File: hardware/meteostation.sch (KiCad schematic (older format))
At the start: 14 parts

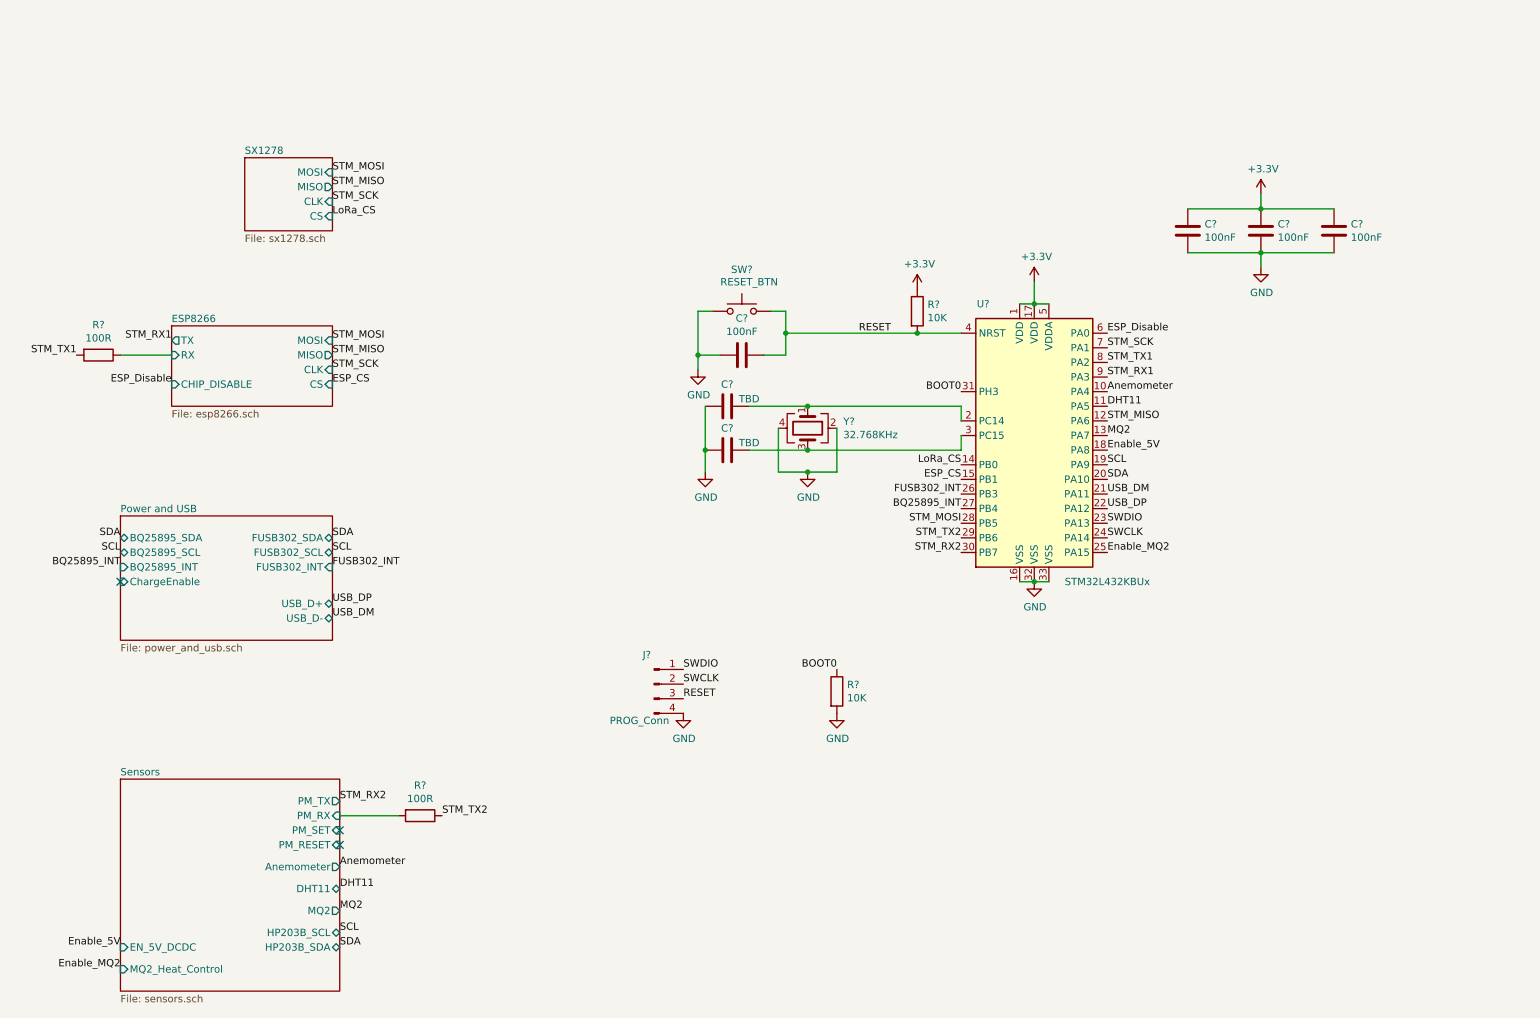
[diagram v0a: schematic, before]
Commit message: Finished sx1278 schematic
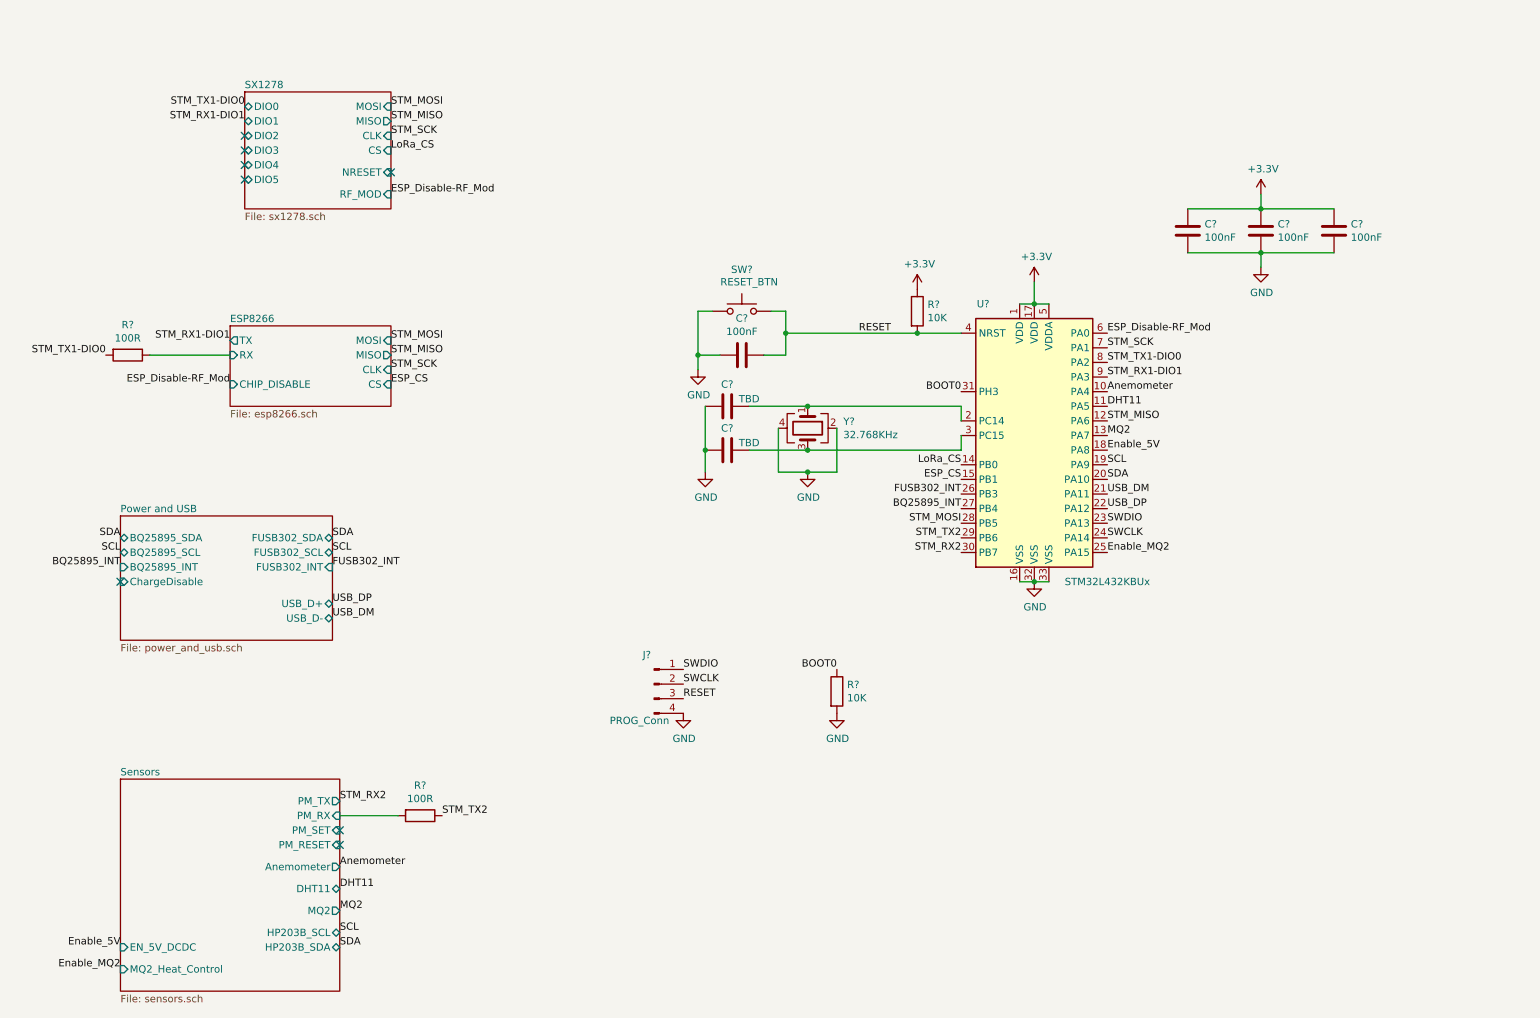
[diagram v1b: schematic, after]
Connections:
- net ESP_Disable renamed ESP_Disable-RF_Mod
- net STM_RX1 renamed STM_RX1-DIO1
- net STM_TX1 renamed STM_TX1-DIO0
- no-connect marks 3 -> 8
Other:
- moved on the sheet: R?
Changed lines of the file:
@@
 RESET
 $Sheet
-S 1850 2850 1100 550
+S 2250 2850 1100 550
 U 60322A2E
 F0 "ESP8266" 50
 F1 "esp8266.sch" 50
-F2 "CHIP_DISABLE" I L 1850 3250 50
-F3 "TX" O L 1850 2950 50
-F4 "RX" I L 1850 3050 50
-F5 "MISO" O R 2950 3050 50
-F6 "CLK" I R 2950 3150 50
-F7 "CS" I R 2950 3250 50
-F8 "MOSI" I R 2950 2950 50
+F2 "CHIP_DISABLE" I L 2250 3250 50
+F3 "TX" O L 2250 2950 50
+F4 "RX" I L 2250 3050 50
+F5 "MISO" O R 3350 3050 50
+F6 "CLK" I R 3350 3150 50
+F7 "CS" I R 3350 3250 50
+F8 "MOSI" I R 3350 2950 50
 $EndSheet
 $Comp
@@
 F3 "BQ25895_SCL" B L 1500 4400 50
 F4 "BQ25895_SDA" B L 1500 4300 50
-F5 "ChargeEnable" I L 1500 4600 50
-F6 "USB_D+" B R 2950 4750 50
-F7 "USB_D-" B R 2950 4850 50
-F8 "FUSB302_INT" I R 2950 4500 50
-F9 "FUSB302_SCL" B R 2950 4400 50
-F10 "FUSB302_SDA" B R 2950 4300 50
+F5 "USB_D+" B R 2950 4750 50
+F6 "USB_D-" B R 2950 4850 50
+F7 "FUSB302_INT" I R 2950 4500 50
+F8 "FUSB302_SCL" B R 2950 4400 50
+F9 "FUSB302_SDA" B R 2950 4300 50
+F10 "ChargeDisable" I L 1500 4600 50
 $EndSheet
 $Sheet
-S 2350 1700 600  500
+S 2350 1250 1000 800
 U 607D8CCB
 F0 "SX1278" 50
 F1 "sx1278.sch" 50
-F2 "MISO" O R 2950 1900 50
-F3 "CLK" I R 2950 2000 50
-F4 "CS" I R 2950 2100 50
-F5 "MOSI" I R 2950 1800 50
+F2 "MISO" O R 3350 1450 50
+F3 "CLK" I R 3350 1550 50
+F4 "CS" I R 3350 1650 50
+F5 "MOSI" I R 3350 1350 50
+F6 "NRESET" I R 3350 1800 50
+F7 "RF_MOD" I R 3350 1950 50
+F8 "DIO0" B L 2350 1350 50
+F9 "DIO1" B L 2350 1450 50
+F10 "DIO2" B L 2350 1550 50
+F11 "DIO3" B L 2350 1650 50
+F12 "DIO4" B L 2350 1750 50
+F13 "DIO5" B L 2350 1850 50
 $EndSheet
 $Sheet
@@
 F12 "Anemometer" O R 3000 6550 50
 $EndSheet
-NoConn ~ 1500 4600
 NoConn ~ 3000 6300
 NoConn ~ 3000 6400
@@
 USB_DM
 Text Label 8250 3100 0    50   ~ 0
-STM_TX1
-Text Label 1200 3050 2    50   ~ 0
-STM_TX1
+STM_TX1-DIO0
 Text Label 8250 3200 0    50   ~ 0
-STM_RX1
+STM_RX1-DIO1
 $Comp
 L Device:R R?
 U 1 1 6065CC0F
-P 1350 3050
+P 1550 3050
 AR Path="/60322A2E/6065CC0F" Ref="R?"  Part="1"
 AR Path="/6065CC0F" Ref="R?"  Part="1"
-F 0 "R?" V 1143 3050 50  0000 C CNN
-F 1 "100R" V 1234 3050 50  0000 C CNN
-F 2 "" V 1280 3050 50  0001 C CNN
-F 3 "~" H 1350 3050 50  0001 C CNN
-	1    1350 3050
+F 0 "R?" V 1343 3050 50  0000 C CNN
+F 1 "100R" V 1434 3050 50  0000 C CNN
+F 2 "" V 1480 3050 50  0001 C CNN
+F 3 "~" H 1550 3050 50  0001 C CNN
+	1    1550 3050
 	0    1    1    0
 $EndComp
-Wire Wire Line
-	1500 3050 1850 3050
-Text Label 1850 2950 2    50   ~ 0
-STM_RX1
 Text Label 7250 4300 2    50   ~ 0
 STM_TX2
@@
 Text Label 7250 4200 2    50   ~ 0
 STM_MOSI
-Text Label 2950 3150 0    50   ~ 0
+Text Label 3350 3150 0    50   ~ 0
 STM_SCK
-Text Label 2950 3050 0    50   ~ 0
+Text Label 3350 3050 0    50   ~ 0
 STM_MISO
-Text Label 2950 2950 0    50   ~ 0
+Text Label 3350 2950 0    50   ~ 0
 STM_MOSI
-Text Label 2950 2000 0    50   ~ 0
+Text Label 3350 1550 0    50   ~ 0
 STM_SCK
-Text Label 2950 1900 0    50   ~ 0
+Text Label 3350 1450 0    50   ~ 0
 STM_MISO
-Text Label 2950 1800 0    50   ~ 0
+Text Label 3350 1350 0    50   ~ 0
 STM_MOSI
 $Comp
@@
 Text Label 8250 3600 0    50   ~ 0
 MQ2
-Text Label 2950 3250 0    50   ~ 0
+Text Label 3350 3250 0    50   ~ 0
 ESP_CS
-Text Label 2950 2100 0    50   ~ 0
+Text Label 3350 1650 0    50   ~ 0
 LoRa_CS
 Text Label 7250 3800 2    50   ~ 0
@@
 Text Label 7250 3900 2    50   ~ 0
 ESP_CS
-Text Label 1850 3250 2    50   ~ 0
-ESP_Disable
 Text Label 8250 2900 0    50   ~ 0
-ESP_Disable
+ESP_Disable-RF_Mod
 Text Label 2950 4500 0    50   ~ 0
 FUSB302_INT
@@
 Text Label 8250 4400 0    50   ~ 0
 Enable_MQ2
+NoConn ~ 1500 4600
+Text Label 2250 3250 2    50   ~ 0
+ESP_Disable-RF_Mod
+Text Label 3350 1950 0    50   ~ 0
+ESP_Disable-RF_Mod
+NoConn ~ 3350 1800
+NoConn ~ 2350 1850
+NoConn ~ 2350 1750
+NoConn ~ 2350 1650
+NoConn ~ 2350 1550
+Text Label 1400 3050 2    50   ~ 0
+STM_TX1-DIO0
+Text Label 2250 2950 2    50   ~ 0
+STM_RX1-DIO1
+Wire Wire Line
+	1700 3050 2250 3050
+Text Label 2350 1350 2    50   ~ 0
+STM_TX1-DIO0
+Text Label 2350 1450 2    50   ~ 0
+STM_RX1-DIO1
 $EndSCHEMATC

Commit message: Select crystals, add HSE for stm32 and fixed some bits
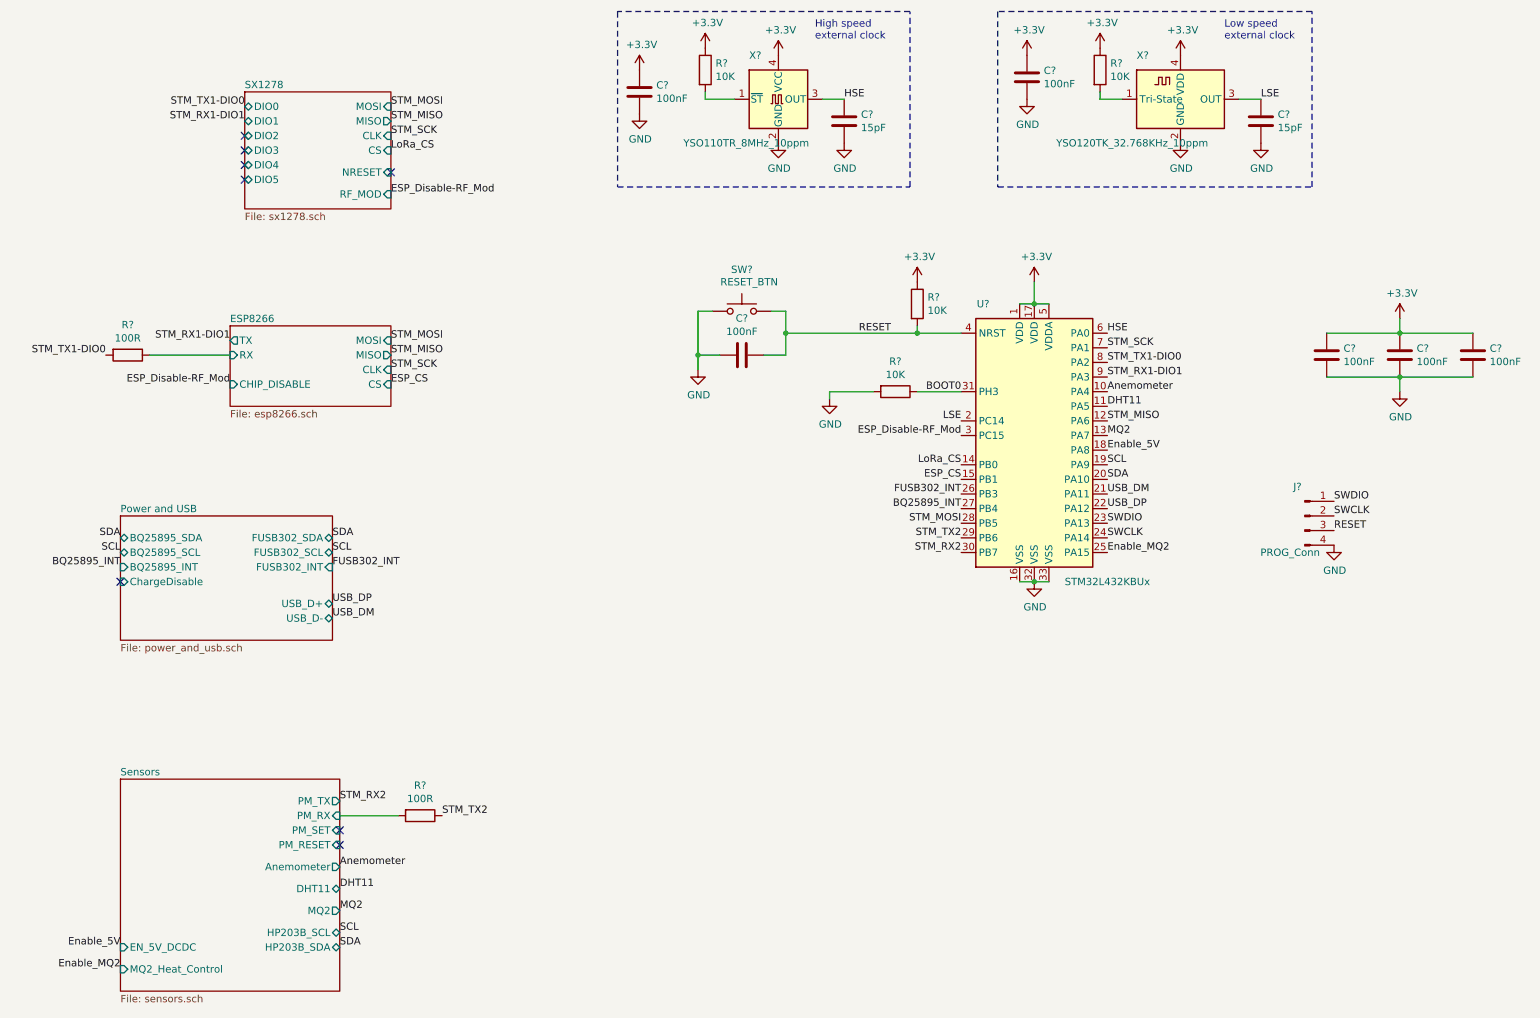
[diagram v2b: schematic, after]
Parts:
- removed C? (x2): TBD, symbol Device:C
- removed R?: 10K, symbol Device:R
- removed Y?: 32.768KHz, symbol Device:Crystal_GND24
- added C? (x2): 100nF, symbol Device:C
- added C? (x2): 15pF, symbol Device:C
- added R? (x3): 10K, symbol Device:R
- added X?: YSO110TR_8MHz_10ppm, Oscillator:Oscillator_SMD_SeikoEpson_SG8002CA-4Pin_7.0x5.0mm, symbol Oscillator:SG-7050CAN
- added X?: YSO120TK_32.768KHz_10ppm, Oscillator:Oscillator_SMD_ECS_2520MV-xxx-xx-4Pin_2.5x2.0mm, symbol Oscillator:ECS-2520MV-xxx-xx
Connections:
- net +3V3: now also C?.1, C?.1, R?.1, R?.1, X?.4 (VCC), X?.4 (VDD)
- net BOOT0: now also R?.1
- net ESP_Disable-RF_Mod: now also U?.3 (PC15); no longer U?.6 (PA0)
- net GND: now also C?.2, C?.2, C?.2, C?.2, R?.2, X?.2 (GND), X?.2 (GND)
- net LSE: now reaches U?.2 (PC14)
- net LSE: now also C?.1, X?.3 (OUT)
- new net: R?.2, X?.1 (~ST)
- new net: R?.2, X?.1 (Tri-State)
- new net HSE: C?.1, U?.6 (PA0), X?.3 (OUT)
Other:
- note added: "High speed\nexternal clock"
- note added: "Low speed\nexternal clock"
- moved on the sheet: C?, J?, R?
